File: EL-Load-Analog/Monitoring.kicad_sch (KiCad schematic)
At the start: 81 parts, among them K2 EE2-5TNU, Q1 2N7002, Q2 2N7002, Q301 2N7002, U1 SN74LVC1G3157DBV, U301 LM833, U302 LM833, U303 OPA189/MCP6V51/LTC2050HV, U304 OPA189/MCP6V51/LTC2050HV, U305 74HCT02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

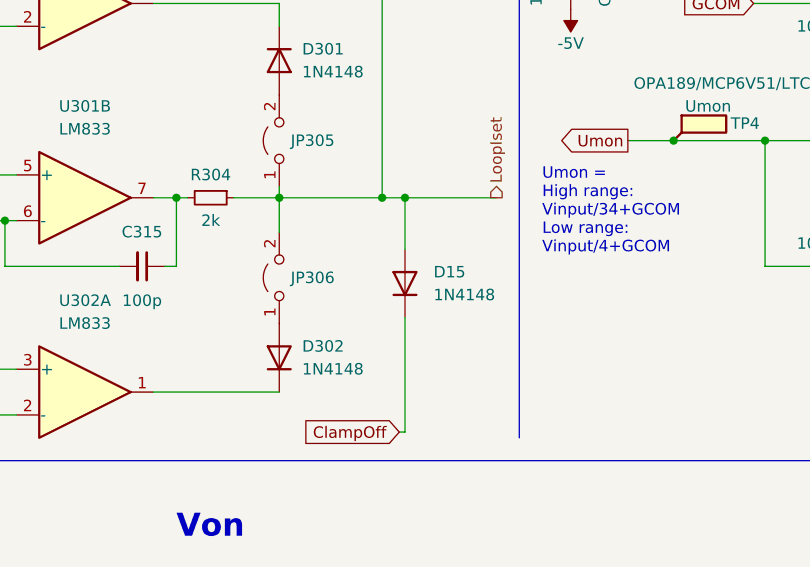
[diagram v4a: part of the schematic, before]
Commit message: Schema changed to 4.1, PCB version E. Modified R44, Remote sense error circtuit had wrong min input.
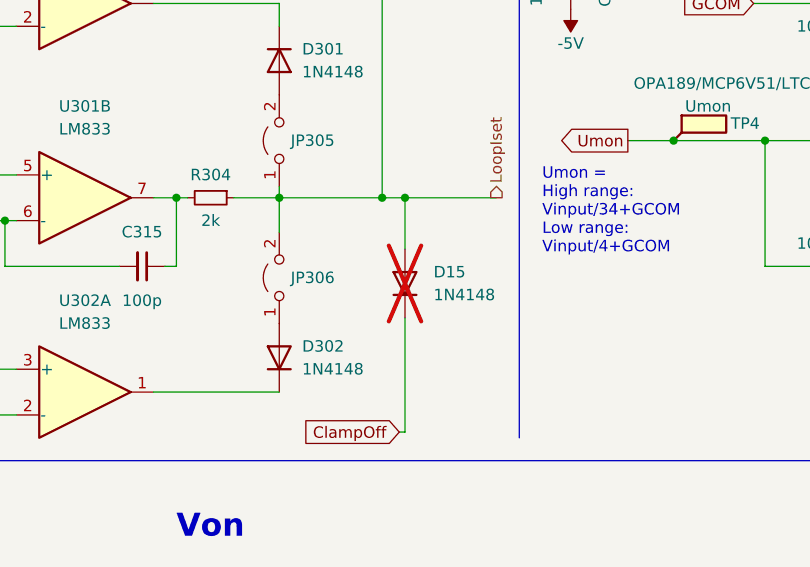
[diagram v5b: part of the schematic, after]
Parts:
- D15: now not fitted; now left out of the parts list
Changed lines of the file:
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@@
   )
   (symbol (lib_id "Diode:1N4148") (at 91.44 65.405 90) (unit 1)
-    (in_bom yes) (on_board yes) (dnp no) (fields_autoplaced)
+    (in_bom no) (on_board yes) (dnp yes) (fields_autoplaced)
     (property "Reference" "D15" (at 94.615 64.135 90)
       (effects (font (size 1.27 1.27)) (justify right))

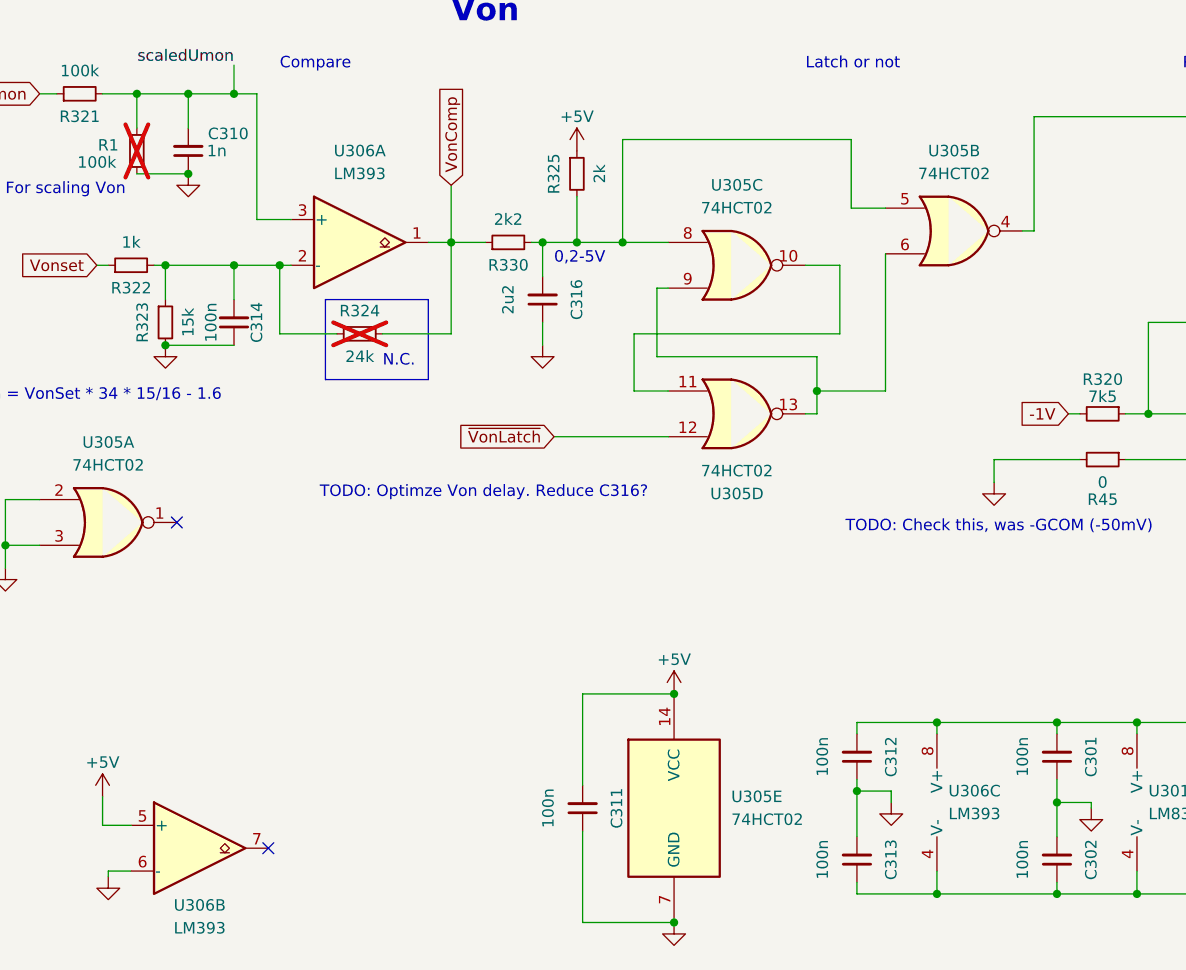
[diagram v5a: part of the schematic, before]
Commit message: Changed comparator to LM393A.
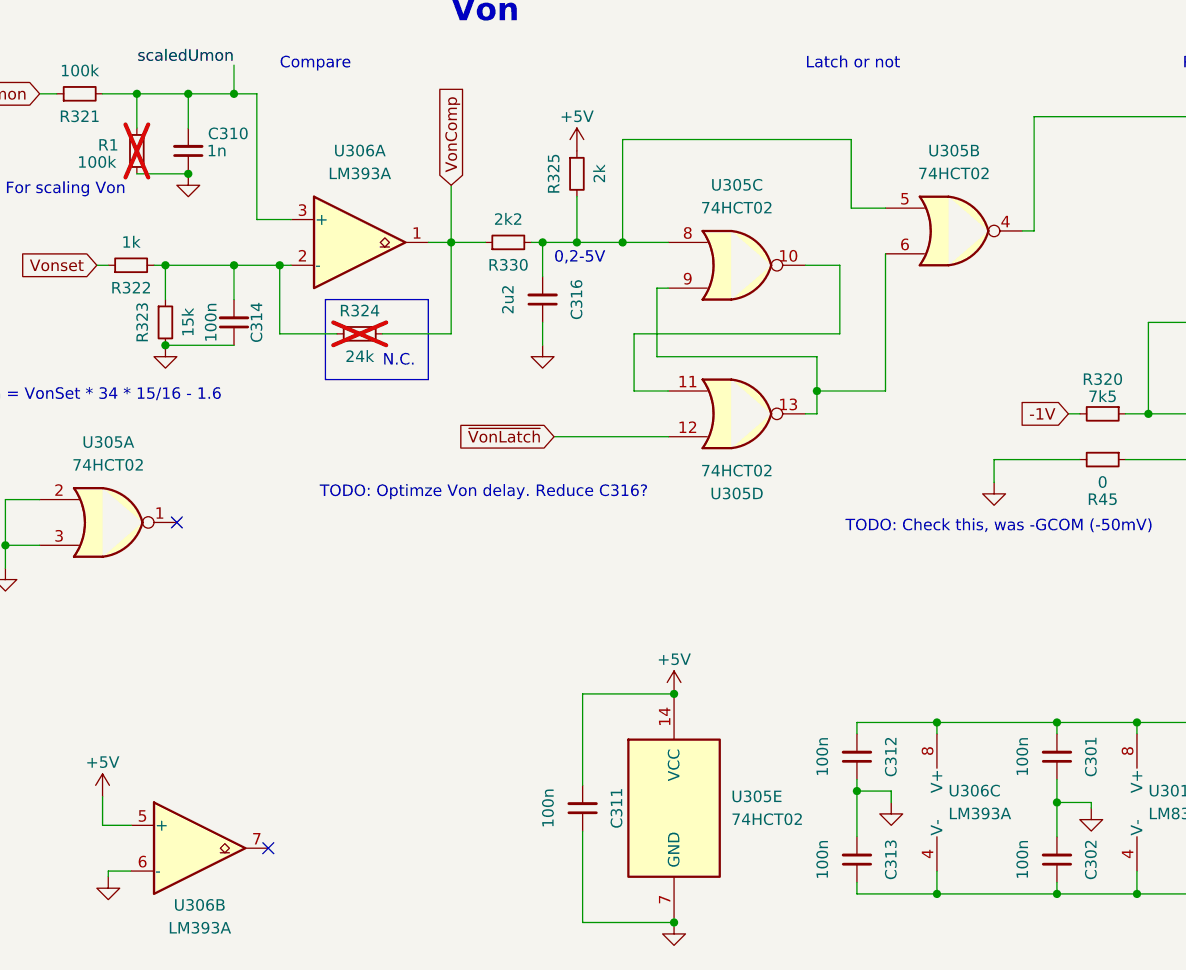
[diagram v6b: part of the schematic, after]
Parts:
- U306: value LM393 -> LM393A; Part Name U_LM393 -> U_LM393A
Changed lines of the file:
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@@
       (effects (font (size 1.27 1.27)))
     )
-    (property "Value" "LM393" (at 55.88 110.49 0)
+    (property "Value" "LM393A" (at 55.88 110.49 0)
       (effects (font (size 1.27 1.27)))
     )
@@
       (effects (font (size 1.27 1.27)) hide)
     )
-    (property "Part Name" "U_LM393 " (at 55.88 118.11 0)
+    (property "Part Name" "U_LM393A" (at 55.88 118.11 0)
       (effects (font (size 1.27 1.27)) hide)
     )
@@
       (effects (font (size 1.27 1.27)))
     )
-    (property "Value" "LM393" (at 38.1 194.31 0)
+    (property "Value" "LM393A" (at 38.1 194.31 0)
       (effects (font (size 1.27 1.27)))
     )
@@
       (effects (font (size 1.27 1.27)) hide)
     )
-    (property "Part Name" "U_LM393 " (at 38.1 185.42 0)
+    (property "Part Name" "U_LM393A" (at 38.1 185.42 0)
       (effects (font (size 1.27 1.27)) hide)
     )
@@
       (effects (font (size 1.27 1.27)) (justify left))
     )
-    (property "Value" "LM393" (at 121.285 181.6099 0)
+    (property "Value" "LM393A" (at 121.285 181.6099 0)
       (effects (font (size 1.27 1.27)) (justify left))
     )
@@
       (effects (font (size 1.27 1.27)) hide)
     )
-    (property "Part Name" "U_LM393 " (at 122.555 180.34 0)
-      (effects (font (size 1.27 1.27)) hide)
-    )
+    (property "Part Name" "U_LM393A" (at 122.555 180.34 0)
+      (effects (font (size 1.27 1.27)) hide)
+    )
